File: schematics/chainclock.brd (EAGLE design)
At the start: 55 x 46.5 mm, 21 parts, among them SW1 ROTARTY_ENCODER

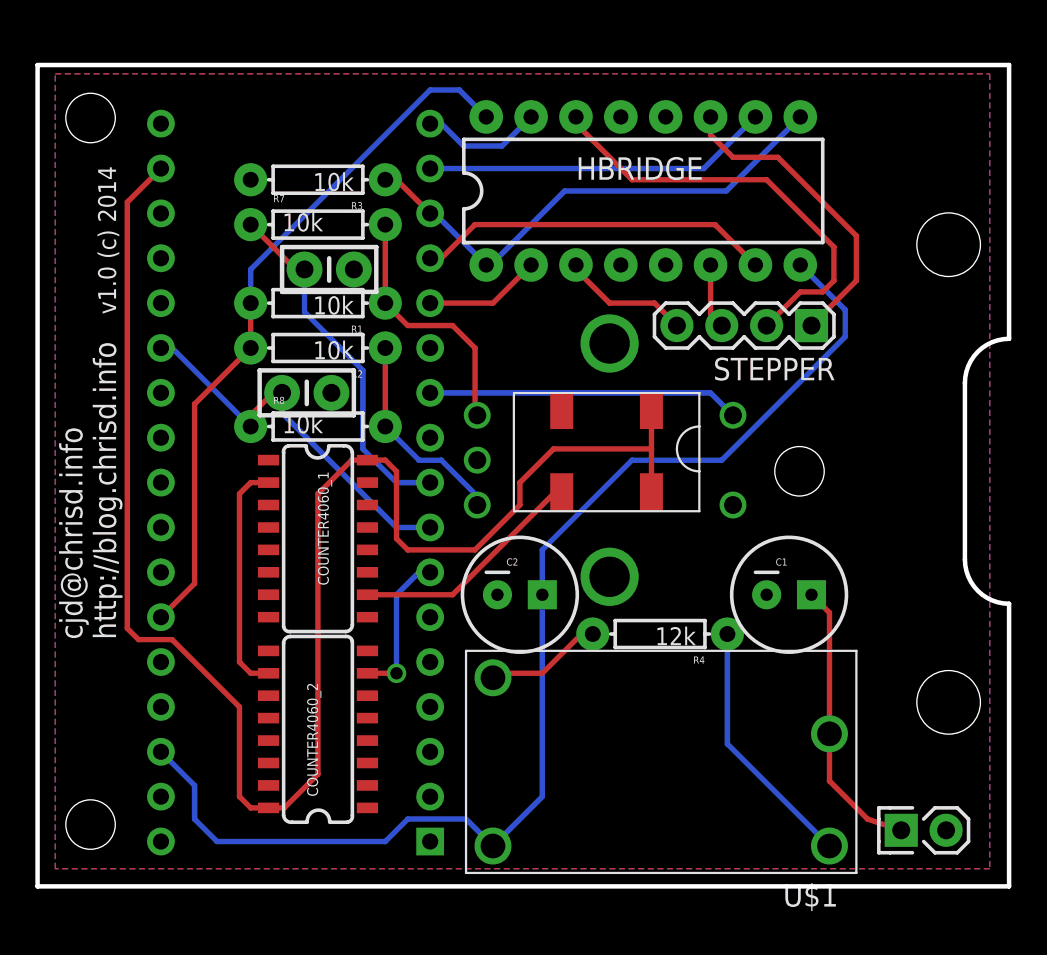
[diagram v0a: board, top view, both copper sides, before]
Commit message: Move encoder off board
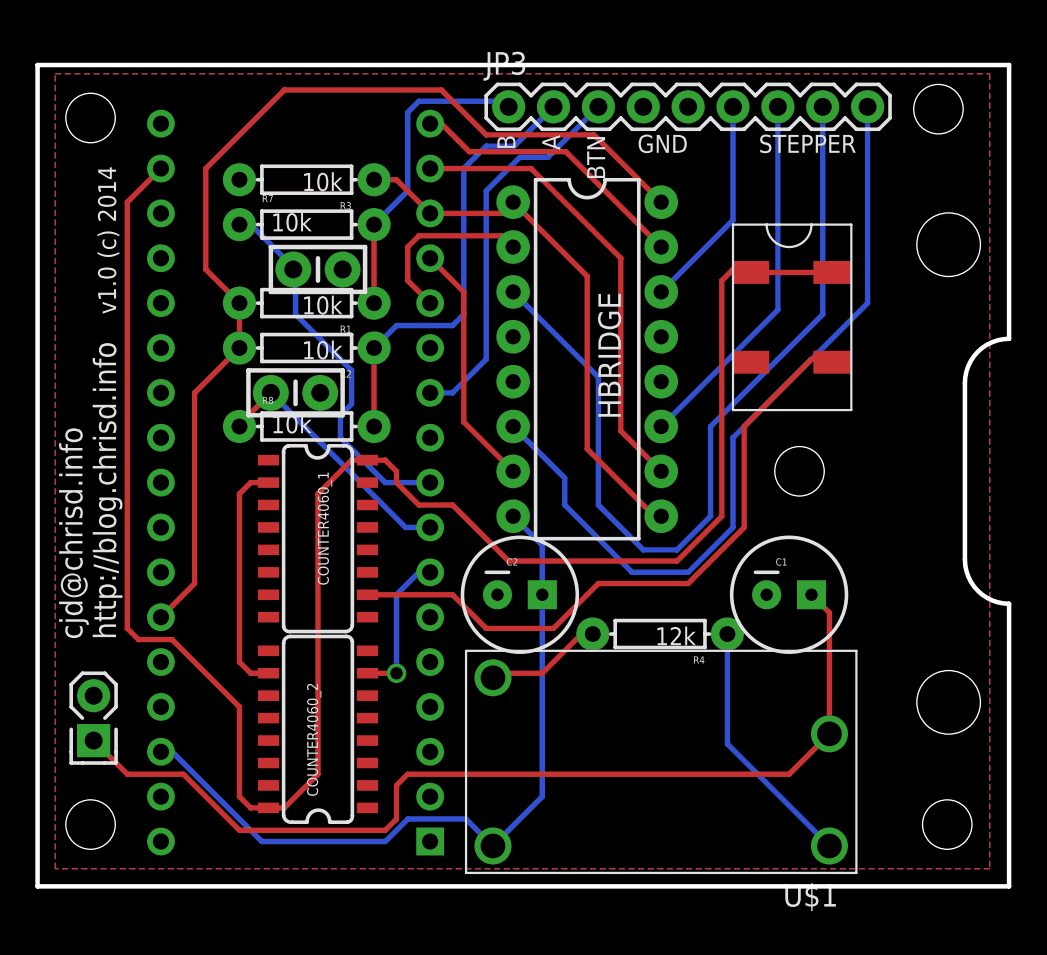
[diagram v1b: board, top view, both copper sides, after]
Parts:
- removed STEPPER: (no value), SparkFun-Connectors:1X04
- removed SW1: ROTARTY_ENCODER, SparkFun-Electromechanical:ROTARY_ENC_PLAIN
- added JP3: M09, SparkFun-Connectors:1X09
- moved JP1 46.0 mm to (3.17, 8.26), turned to 90 degrees
- moved HBRIDGE 10.0 mm to (31.1, 29.8), turned to 270 degrees
- moved SG3040JC 9.71 mm to (39.4, 37.5), turned to 270 degrees
- moved C6 0.64 mm to (15.9, 34.9)
- moved C5 0.63 mm to (14.6, 27.9)
- moved R1 0.63 mm to (15.2, 33.0)
- moved R2 0.63 mm to (15.2, 30.5)
- moved R3 0.63 mm to (15.2, 40.0)
- moved R7 0.63 mm to (15.2, 37.5)
- moved R8 0.63 mm to (15.2, 26.0)
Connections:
- removed net N$2: R1.P$1, R7.P$2, SW1.B
- removed net N$5: R2.P$1, R8.P$2, SW1.A
- new net RENA: JP3.2, R2.P$1, R8.P$2
- new net RENB: JP3.1, R1.P$1, R7.P$2
- net 1Y: now also JP3.8; no longer STEPPER.4
- net 2Y: now also JP3.9; no longer STEPPER.3
- net 3Y: now also JP3.7; no longer STEPPER.1
- net 4Y: now also JP3.6; no longer STEPPER.2
- net GND: now also JP3.4, JP3.5; no longer SW1.C, SW1.SW-
- net RENBTN: now also JP3.3; no longer SW1.SW+
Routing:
- net 2Y: track 3.69 -> 44.8 mm
- net 1Y: track 7.28 -> 48.1 mm
- net VBATT: track 16.0 -> 55.4 mm
- net VIN: track 68.4 -> 42.6 mm
- net RENA: track 0.00 -> 25.1 mm
- net RTC: track 13.8 -> 36.8 mm
- net 5VREG: track 40.0 -> 58.3 mm
- net RENB: track 0.00 -> 17.7 mm
- net 3V3: track 93.2 -> 108.8 mm
- net N$2: track 14.4 -> 0.00 mm
- net 4Y: track 24.6 -> 12.2 mm
- net N$5: track 11.8 -> 0.00 mm
- net 4A: track 6.92 -> 16.0 mm
- net RENCA: track 21.4 -> 15.0 mm
- net 3A: track 19.6 -> 25.9 mm
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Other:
- board text added: "A"
- board text added: "B"
- board text added: "BTN"
- board text added: "GND"
- board text added: "STEPPER"

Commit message: Updates to chainlock
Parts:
- removed C1, C2: (no value), SparkFun-Capacitors:CPOL-RADIAL-100UF-25V
- added C3, C4: 100uf, SparkFun-Capacitors:CAP-PTH-SMALL-KIT
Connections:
- net GND: now also C3.2, C4.2; no longer C1.2, C2.2
- net VBATT: now also C3.1; no longer C1.1
- net VIN: now also C4.1; no longer C2.1
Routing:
- net RTC: track 36.8 -> 35.2 mm
- net VBATT: track 55.4 -> 54.4 mm
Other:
- board text added: "cjd@chrisd.info blog.chrisd.info"
- board text removed: "cjd@chrisd.info http://blog.chrisd.info"
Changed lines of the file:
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@@
 <setting verticaltext="up"/>
 </settings>
-<grid distance="0.025" unitdist="inch" unit="inch" style="lines" multiple="1" display="yes" altdistance="0.025" altunitdist="inch" altunit="inch"/>
+<grid distance="0.025" unitdist="inch" unit="mm" style="lines" multiple="1" display="yes" altdistance="0.025" altunitdist="inch" altunit="inch"/>
 <layers>
 <layer number="1" name="Top" color="4" fill="1" visible="yes" active="yes"/>
@@
 <board>
 <plain>
-<hole x="3" y="3.5" drill="2.8"/>
-<hole x="3" y="43.5" drill="2.8"/>
+<hole x="3" y="3.5" drill="3"/>
+<hole x="3" y="43.5" drill="3"/>
 <hole x="43.135" y="23.5" drill="2.8"/>
 <text x="4.445" y="13.97" size="1.27" layer="21" rot="R90">cjd@chrisd.info
-http://blog.chrisd.info</text>
+blog.chrisd.info</text>
 <wire x1="0" y1="0" x2="0" y2="46.5" width="0.254" layer="20"/>
 <wire x1="0" y1="46.5" x2="55" y2="46.5" width="0.254" layer="20"/>
@@
 <text x="28.575" y="42.545" size="1.016" layer="21" rot="R270">A</text>
 <text x="31.115" y="42.545" size="1.016" layer="21" rot="R270">BTN</text>
-<hole x="51.5" y="3.5" drill="2.8"/>
-<hole x="51" y="44" drill="2.8"/>
+<hole x="51.5" y="3.5" drill="3"/>
+<hole x="51.5" y="43.5" drill="3"/>
 </plain>
 <attributes>
@@
 <element name="U$4" library="ChrisD" package="ARDUINO_PRO_MICRO" value="ARDUINO_PRO_MICRO" x="23.495" y="46.99" rot="R180"/>
 <element name="U$1" library="desjardins" package="EUU4" value="PTN0405C" x="46.355" y="13.335" rot="R180"/>
-<element name="C1" library="SparkFun-Capacitors" package="CPOL-RADIAL-100UF-25V" value="" x="42.545" y="16.51"/>
-<element name="C2" library="SparkFun-Capacitors" package="CPOL-RADIAL-100UF-25V" value="" x="27.305" y="16.51"/>
 <element name="R4" library="SparkFun-Resistors" package="AXIAL-0.3EZ" value="12k" x="35.2425" y="14.2875" rot="R180"/>
 <element name="JP1" library="desjardins" package="MOLEX-1X2" value="M02POLAR" x="3.175" y="8.255" rot="R90"/>
@@
 <element name="COUNTER4060_2" library="desjardins" package="SO016" value="4060SOIC16" x="15.875" y="8.89" rot="R90"/>
 <element name="JP3" library="SparkFun-Connectors" package="1X09" value="M09" x="26.67" y="44.1325"/>
+<element name="C3" library="SparkFun-Capacitors" package="CAP-PTH-SMALL-KIT" value="100uf" x="43.18" y="14.605">
+<attribute name="PROD_ID" value="CAP-08370" x="43.18" y="14.605" size="1.778" layer="27" display="off"/>
+</element>
+<element name="C4" library="SparkFun-Capacitors" package="CAP-PTH-SMALL-KIT" value="100uf" x="27.305" y="14.605" rot="R180">
+<attribute name="PROD_ID" value="CAP-08370" x="27.305" y="14.605" size="1.778" layer="27" rot="R180" display="off"/>
+</element>
 </elements>
 <signals>
@@
 <vertex x="53.905" y="1"/>
 </polygon>
-<contactref element="C2" pad="2"/>
-<contactref element="C1" pad="2"/>
 <contactref element="JP1" pad="2"/>
 <contactref element="COUNTER4060_1" pad="8"/>
@@
 <contactref element="JP3" pad="4"/>
 <contactref element="JP3" pad="5"/>
+<contactref element="C3" pad="2"/>
+<contactref element="C4" pad="2"/>
 </signal>
 <signal name="3V30">
@@
 <contactref element="SG3040JC" pad="3"/>
 <contactref element="COUNTER4060_1" pad="10"/>
-<wire x1="23.495" y1="16.51" x2="18.675" y2="16.51" width="0.3048" layer="1"/>
 <wire x1="43.815" y1="29.845" x2="44.165" y2="29.845" width="0.3048" layer="1"/>
 <wire x1="44.165" y1="29.845" x2="44.97" y2="29.675" width="0.3048" layer="1"/>
 <wire x1="40.005" y1="26.035" x2="43.815" y2="29.845" width="0.3048" layer="1"/>
 <wire x1="40.005" y1="26.035" x2="40.005" y2="20.32" width="0.3048" layer="1"/>
-<wire x1="23.495" y1="16.51" x2="25.4" y2="14.605" width="0.3048" layer="1"/>
-<wire x1="25.4" y1="14.605" x2="29.21" y2="14.605" width="0.3048" layer="1"/>
-<wire x1="29.21" y1="14.605" x2="31.75" y2="17.145" width="0.3048" layer="1"/>
-<wire x1="31.75" y1="17.145" x2="36.83" y2="17.145" width="0.3048" layer="1"/>
-<wire x1="36.83" y1="17.145" x2="40.005" y2="20.32" width="0.3048" layer="1"/>
+<wire x1="40.005" y1="20.32" x2="36.195" y2="16.51" width="0.3048" layer="1"/>
+<wire x1="36.195" y1="16.51" x2="18.675" y2="16.51" width="0.3048" layer="1"/>
 </signal>
 <signal name="VIN">
@@
 <contactref element="HBRIDGE" pad="8"/>
 <contactref element="U$1" pad="4"/>
-<contactref element="C2" pad="1"/>
 <wire x1="24.257" y1="3.81" x2="25.781" y2="2.286" width="0.3048" layer="16"/>
 <wire x1="19.685" y1="2.54" x2="20.955" y2="3.81" width="0.3048" layer="16"/>
 <wire x1="20.955" y1="3.81" x2="24.257" y2="3.81" width="0.3048" layer="16"/>
-<wire x1="28.575" y1="16.51" x2="28.575" y2="5.08" width="0.3048" layer="16"/>
-<wire x1="28.575" y1="5.08" x2="25.781" y2="2.286" width="0.3048" layer="16"/>
-<wire x1="28.575" y1="16.51" x2="28.575" y2="19.304" width="0.3048" layer="16"/>
-<wire x1="28.575" y1="19.304" x2="26.924" y2="20.955" width="0.3048" layer="16"/>
 <wire x1="19.685" y1="2.54" x2="12.7" y2="2.54" width="0.3048" layer="16"/>
 <wire x1="12.7" y1="2.54" x2="7.62" y2="7.62" width="0.3048" layer="16"/>
 <wire x1="7.62" y1="7.62" x2="6.985" y2="7.62" width="0.3048" layer="16"/>
+<contactref element="C4" pad="1"/>
+<wire x1="25.781" y1="2.286" x2="28.575" y2="5.08" width="0.3048" layer="16"/>
+<wire x1="28.575" y1="5.08" x2="28.575" y2="14.478" width="0.3048" layer="16"/>
+<wire x1="28.575" y1="14.478" x2="28.702" y2="14.605" width="0.3048" layer="16"/>
+<wire x1="26.924" y1="20.955" x2="26.924" y2="20.701" width="0.3048" layer="16"/>
+<wire x1="26.924" y1="20.701" x2="28.575" y2="19.05" width="0.3048" layer="16"/>
+<wire x1="28.575" y1="19.05" x2="28.575" y2="14.732" width="0.3048" layer="16"/>
+<wire x1="28.575" y1="14.732" x2="28.702" y2="14.605" width="0.3048" layer="16"/>
 </signal>
 <signal name="REF">
@@
 <contactref element="R4" pad="P$2"/>
 <contactref element="U$1" pad="3"/>
-<wire x1="31.4325" y1="14.2875" x2="30.7975" y2="14.2875" width="0.3048" layer="1"/>
-<wire x1="30.7975" y1="14.2875" x2="28.575" y2="12.065" width="0.3048" layer="1"/>
-<wire x1="28.575" y1="12.065" x2="26.035" y2="12.065" width="0.3048" layer="1"/>
-<wire x1="26.035" y1="12.065" x2="25.781" y2="11.811" width="0.3048" layer="1"/>
+<wire x1="25.781" y1="11.811" x2="28.956" y2="11.811" width="0.3048" layer="1"/>
+<wire x1="28.956" y1="11.811" x2="31.4325" y2="14.2875" width="0.3048" layer="1"/>
 </signal>
 <signal name="N$1">
@@
 <signal name="VBATT">
 <contactref element="U$1" pad="2"/>
-<contactref element="C1" pad="1"/>
 <contactref element="JP1" pad="1"/>
-<wire x1="44.831" y1="8.636" x2="44.831" y2="15.494" width="0.3048" layer="1"/>
-<wire x1="44.831" y1="15.494" x2="43.815" y2="16.51" width="0.3048" layer="1"/>
 <wire x1="3.175" y1="8.255" x2="5.08" y2="6.35" width="0.3048" layer="1"/>
 <wire x1="5.08" y1="6.35" x2="8.255" y2="6.35" width="0.3048" layer="1"/>
@@
 <wire x1="20.955" y1="6.35" x2="42.545" y2="6.35" width="0.3048" layer="1"/>
 <wire x1="42.545" y1="6.35" x2="44.831" y2="8.636" width="0.3048" layer="1"/>
+<contactref element="C3" pad="1"/>
+<wire x1="44.831" y1="8.636" x2="44.704" y2="8.636" width="0.3048" layer="1"/>
+<wire x1="44.704" y1="8.636" x2="41.91" y2="11.43" width="0.3048" layer="1"/>
+<wire x1="41.91" y1="11.43" x2="41.91" y2="14.478" width="0.3048" layer="1"/>
+<wire x1="41.91" y1="14.478" x2="41.783" y2="14.605" width="0.3048" layer="1"/>
 </signal>
 <signal name="Q13">

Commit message: Originize the routin
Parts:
- moved C6 5.75 mm to (15.2, 29.2)
- moved R8 5.71 mm to (15.2, 31.8)
- moved R2 3.81 mm to (15.2, 34.3)
- moved R1 3.81 mm to (15.2, 36.8)
- moved R3 1.90 mm to (15.2, 41.9)
- moved R7 1.90 mm to (15.2, 39.4)
- moved C5 1.42 mm to (15.2, 26.7)
- moved R4 0.63 mm to (35.2, 14.9)
- turned C3 to 180 degrees
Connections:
- removed net GND0: U$4.P6
- removed net GND1: U$4.P31
- net GND: now also U$4.P31, U$4.P6
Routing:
- net 5VREG: track 58.3 -> 52.8 mm
- net RENCB: track 21.5 -> 25.3 mm
- net RENB: track 17.7 -> 13.9 mm
- net 3V3: track 108.8 -> 106.1 mm
- net RENCA: track 15.0 -> 17.7 mm
- net RENA: track 25.1 -> 22.7 mm
- net VBATT: track 54.4 -> 52.1 mm
- net EN: track 30.4 -> 31.6 mm
- net VOADJ: track 6.68 -> 7.31 mm
- net N$1: track 14.4 -> 15.0 mm

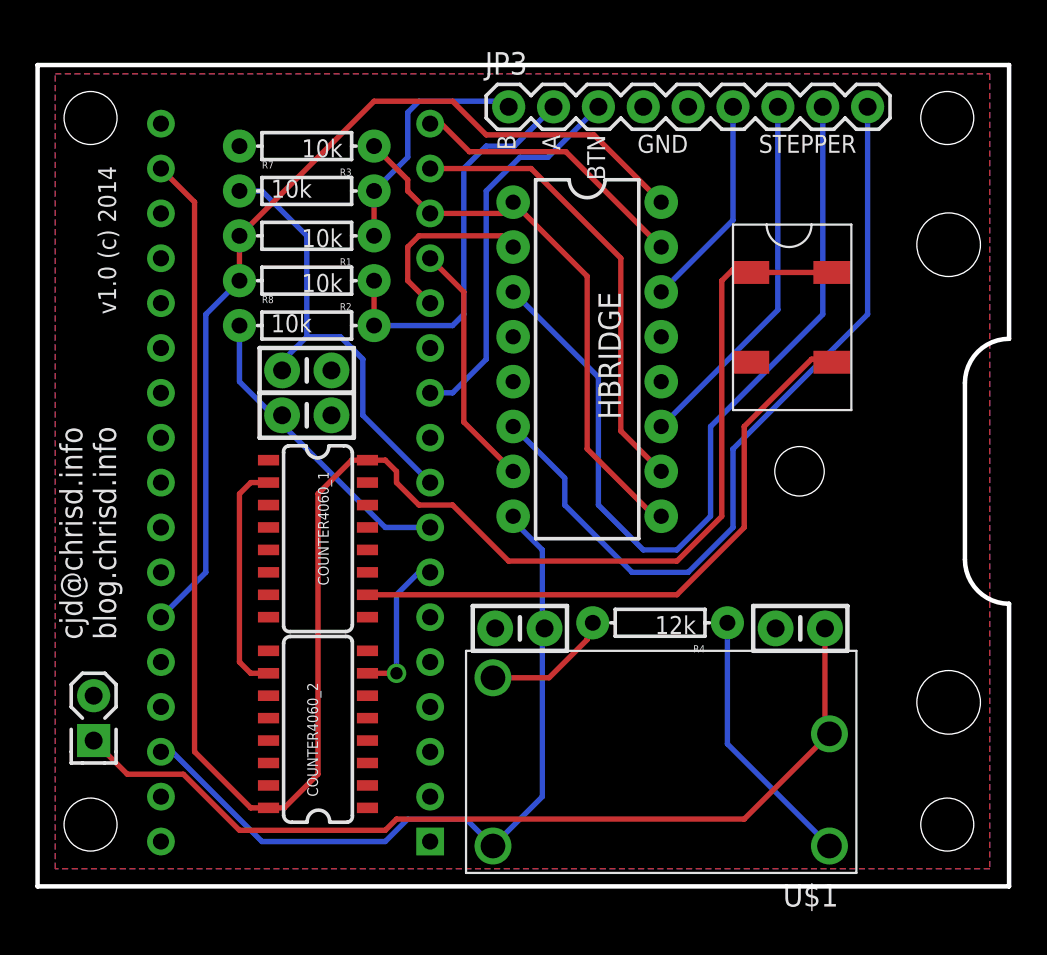
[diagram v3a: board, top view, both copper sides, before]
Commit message: Update layout of chainclock
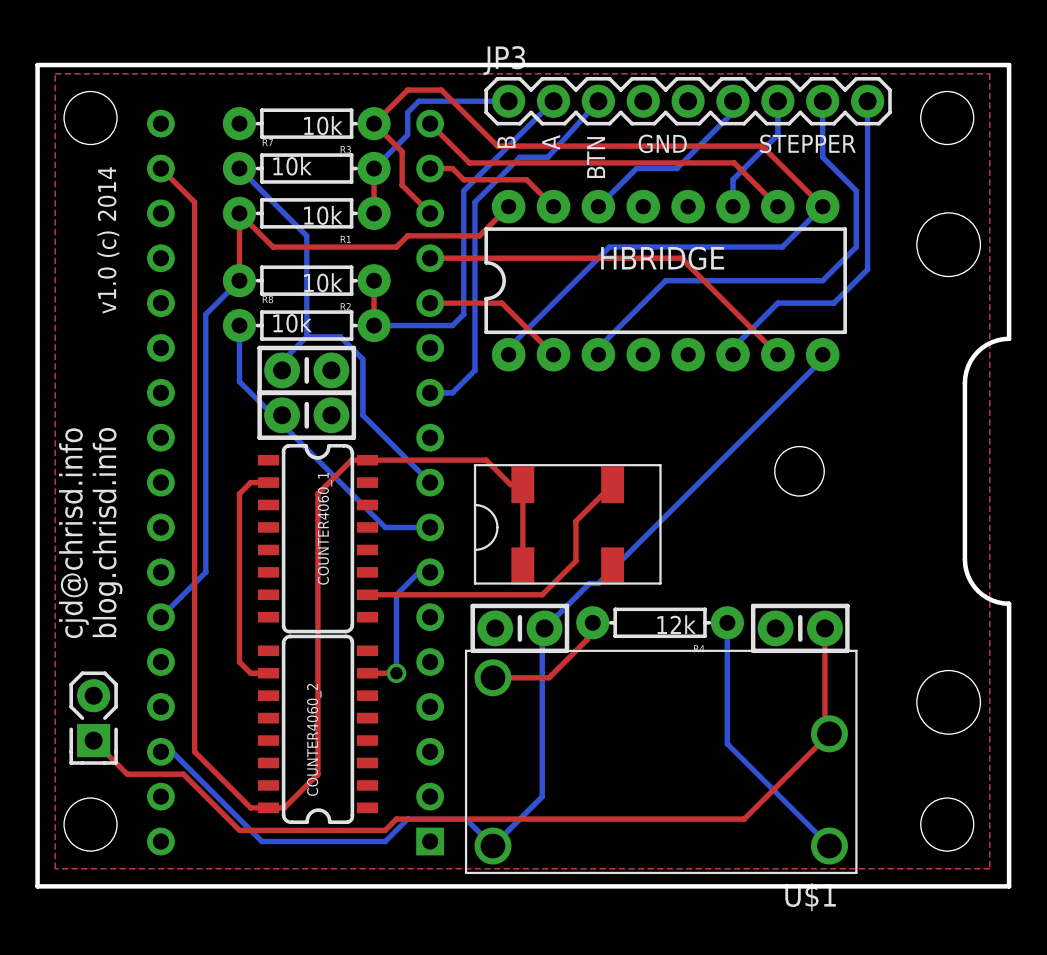
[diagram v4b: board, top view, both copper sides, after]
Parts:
- moved SG3040JC 25.0 mm to (24.8, 17.1), turned to 0 degrees
- moved HBRIDGE 6.29 mm to (35.6, 34.3), turned to 0 degrees
- moved R1 1.27 mm to (15.2, 38.1)
- moved R3 1.27 mm to (15.2, 43.2)
- moved R7 1.27 mm to (15.2, 40.6)
- moved JP3 0.32 mm to (26.7, 44.5)
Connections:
- net 3A: now also U$4.P17; no longer U$4.P16
- net 4A: now also U$4.P16; no longer U$4.P17
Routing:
- net 3V3: track 106.1 -> 76.3 mm
- net 2Y: track 44.8 -> 19.4 mm
- net EN: track 31.6 -> 56.8 mm
- net 1Y: track 48.1 -> 26.4 mm
- net RTC: track 35.2 -> 17.8 mm
- net VIN: track 42.7 -> 57.9 mm
- net 3Y: track 20.8 -> 7.02 mm
- net 5VREG: track 52.8 -> 41.7 mm
- net 4A: track 16.0 -> 7.88 mm
- net 2A: track 14.0 -> 21.9 mm
- net 3A: track 25.9 -> 21.6 mm
- net 1A: track 10.2 -> 8.19 mm
- net 4Y: track 12.2 -> 10.5 mm
- net RENB: track 13.9 -> 12.5 mm
- net RENA: track 22.7 -> 22.1 mm
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
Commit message: First pass
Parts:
- added JP2: M09, SparkFun-Connectors:1X09
- moved U$3 20.3 mm to (49.7, 13.0), flipped to the top, turned to 90 degrees
- renumbered U$1 to PTN04050
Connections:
- new net A0: JP2.2, U$4.P21
- new net A1: JP2.3, U$4.P22
- new net A2: JP2.4, U$4.P23
- new net A3: JP2.5, U$4.P24
- new net A4: JP2.6, U$4.P25
- new net A5: JP2.7, U$4.P26
- new net D13: JP2.1, U$4.P18
- net 5VREG: now also JP2.9
- net GND: now also JP2.8
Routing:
- net D13: track 0.00 -> 6.26 mm
- net 5VREG: track 41.7 -> 45.6 mm
- net A5: track 0.00 -> 2.86 mm
- net A4: track 0.00 -> 2.86 mm
- net A3: track 0.00 -> 2.86 mm
- net A2: track 0.00 -> 2.86 mm
- net A1: track 0.00 -> 2.86 mm
- net A0: track 0.00 -> 2.86 mm
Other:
- board text added: "5v"
- board text added: "cjd@chrisd.info blog.chrisd.info v1.0 (c) 2015"
- board text removed: "cjd@chrisd.info blog.chrisd.info"
- board text removed: "v1.0 (c) 2014"
